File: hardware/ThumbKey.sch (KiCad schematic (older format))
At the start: 2 parts

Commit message: Replace 1.5u with 2u thumb keys
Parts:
- S61: footprint keyboard-modules:CHERRY_PCB_150H -> keyboard-modules:CHERRY_PCB_200V
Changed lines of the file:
@@
 $Descr A4 11693 8268
 encoding utf-8
-Sheet 65 66
+Sheet 63 66
 Title ""
 Date ""
@@
 F 0 "S61" H 2650 1500 60  0000 R CNN
 F 1 "SPST" H 2250 1500 60  0000 C CNN
-F 2 "keyboard-modules:CHERRY_PCB_150H" H 2400 1650 60  0001 C CNN
+F 2 "keyboard-modules:CHERRY_PCB_200V" H 2400 1650 60  0001 C CNN
 F 3 "" H 2400 1650 60  0001 C CNN
 	1    2400 1550

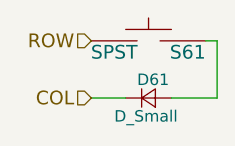
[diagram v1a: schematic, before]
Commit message: Fix diodes, Add board edge
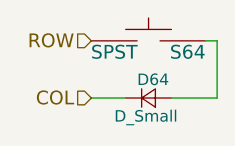
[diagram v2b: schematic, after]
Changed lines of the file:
@@
 AR Path="/5947FBED/59512178/5950FE13" Ref="S63"  Part="1"
 AR Path="/5947FBED/595128C4/5950FE13" Ref="S64"  Part="1"
-F 0 "S61" H 2650 1500 60  0000 R CNN
+F 0 "S64" H 2650 1500 60  0000 R CNN
 F 1 "SPST" H 2250 1500 60  0000 C CNN
 F 2 "keyboard-modules:CHERRY_PCB_200V" H 2400 1650 60  0001 C CNN
@@
 AR Path="/5947FBED/59512178/5950FE1A" Ref="D63"  Part="1"
 AR Path="/5947FBED/595128C4/5950FE1A" Ref="D64"  Part="1"
-F 0 "D61" H 2350 1880 50  0000 L CNN
+F 0 "D64" H 2350 1880 50  0000 L CNN
 F 1 "D_Small" H 2250 1720 50  0000 L CNN
 F 2 "Diodes_SMD:D_1206" V 2400 1800 50  0001 C CNN
